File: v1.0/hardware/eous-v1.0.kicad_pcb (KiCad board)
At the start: 2 copper layers, 79 parts, among them J1 Screw_Terminal_01x02, J2 Conn_01x03, J3 Conn_01x03, SW1 TS-1088-AR02016, SW2 TS-1088-AR02016, U1 BQ25883RGER, U2 ICM-45686, U3 STM32F722RETx, U4 BMP580, U5 TPS63070RNMR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

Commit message: pcb edits before routing
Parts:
- moved C25 72.0 mm to (138.4, 52.1)
- moved C26 72.0 mm to (135.1, 69.2)
- moved C29 72.0 mm to (128.6, 58.6)
- moved C32 72.0 mm to (145.9, 60.4)
- moved L4 72.0 mm to (128.9, 57.1)
- moved C23 72.0 mm to (133.8, 68.9)
- moved C24 72.0 mm to (136.3, 52.1)
- moved C27 72.0 mm to (130.0, 64.2)
- moved C31 72.0 mm to (137.3, 51.8)
- moved U3 72.0 mm to (137.3, 60.6)
- moved C28 72.0 mm to (145.7, 61.5)
- moved C30 72.0 mm to (134.9, 70.4)
- moved R9 72.0 mm to (141.9, 54.3)
- moved USB1 16.3 mm to (146.2, 75.4)
- moved R1 16.3 mm to (144.6, 71.7)
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
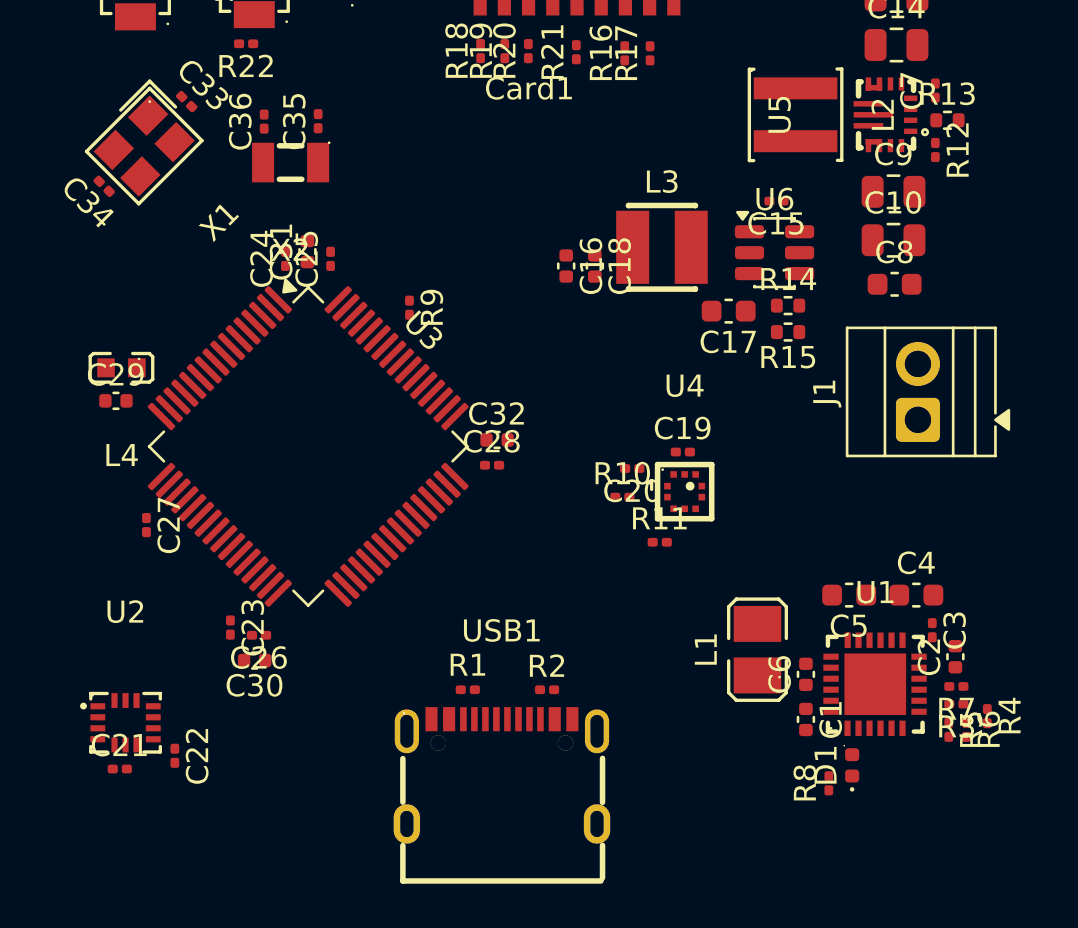
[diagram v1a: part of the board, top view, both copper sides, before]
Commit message: update board setup
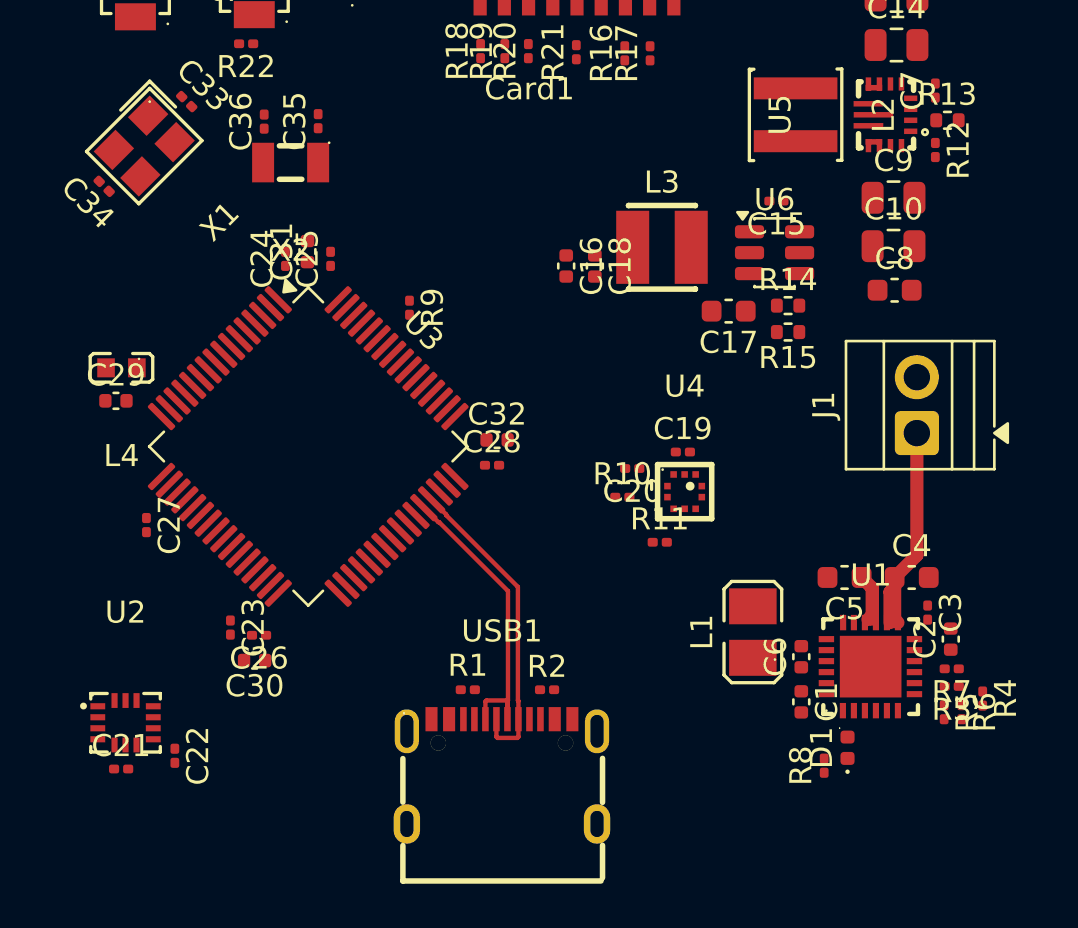
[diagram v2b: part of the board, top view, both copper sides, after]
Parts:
- moved C4 0.83 mm to (164.8, 66.6)
- moved C5 0.83 mm to (161.7, 66.6)
- moved D1 0.83 mm to (161.8, 74.3)
- moved C3 0.83 mm to (165.5, 68.2)
- moved R4 0.83 mm to (168.0, 72.1)
- moved C1 0.83 mm to (159.8, 72.2)
- moved C2 0.83 mm to (166.5, 69.4)
- moved C6 0.83 mm to (159.8, 70.2)
- moved R6 0.83 mm to (167.0, 72.7)
- moved R8 0.83 mm to (160.8, 75.2)
- moved U1 0.83 mm to (162.9, 70.7)
- moved L1 0.83 mm to (157.6, 69.1)
- moved R3 0.83 mm to (166.6, 71.5)
- moved R5 0.83 mm to (166.2, 72.7)
- moved R7 0.83 mm to (166.6, 70.8)
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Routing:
- net /USB_DP: track 0.00 -> 14.2 mm
- net /USB_DN: track 0.00 -> 13.9 mm
- net BAT+: track 0.00 -> 11.2 mm
- net VSYS: track 0.00 -> 3.59 mm
